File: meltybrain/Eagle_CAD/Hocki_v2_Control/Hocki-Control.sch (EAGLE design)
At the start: 152 parts, among them J1 SM03B-SRSS-TB(LF)(SN), J2 SM04B-SRSS-TB(LF)(SN), J3 SM02B-SRSS-TB(LF)(SN), J4 SM04B-SRSS-TB(LF)(SN), J5 SM03B-SRSS-TB(LF)(SN), J6 SM03B-SRSS-TB(LF)(SN), U1 AP63200, U10 LMH6612MAX/NOPB, U11 TLV3502AIDCNR, U12 LMH6612MAX/NOPB, U13 TMP235A4DCKR, U14 ADXL375, U15 NL27WZ32USG, U16 ADXL375, U17 ADXL375, U18 NL27WZ32USG, U19 ADXL375, U2 TEENSY_4.1, U20 LMV358, U21 LMV358, U22 HMC1052L-TR, U23 LMV358, U24 IRF7509, U3 AP2210K-5.0TRG1, U4 AP2210K-3.3TRG1, U5 74AHC1G04GW,125, U6 LDL212PU50R, U7 LMH6612MAX/NOPB, U8 LMH6612MAX/NOPB, U9 TMUX1219DCKR

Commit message: Moving v2 to a new directory to avoid merge conflicts and allow both versions to coexist in master
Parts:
- removed C52: 1000pF, rcl:C-USC0805
- removed J3: SM02B-SRSS-TB(LF)(SN), Hocki_Library:SM02B-SRSS-TB(LF)(SN)
- removed R37, R38, R41: 4.99k, rcl:R-US_R0603
- removed R42, R43, R44: 499k, rcl:R-US_R0603
- added C56: 0.1uF, rcl:C-USC0603
- added FB1: MPZ1608R391ATD25, Hocki_Library:MPZ1608R391ATD25
- added J7, J8: SM02B-SRSS-TB(LF)(SN), Hocki_Library:SM02B-SRSS-TB(LF)(SN)
- C44: value 1000pF -> 0.1uF; device rcl:C-USC0805 -> rcl:C-USC0603
- CN1: value (none) -> JST_2PIN
- R33: value 499k -> 49.9
- R36: value 4.99k -> 49.9
- U20: value LMV358 -> AD8426ACPZ-WP; device Hocki_Library:LMV358 -> Hocki_Library:AD8426ACPZ-WP
- U21, U23: value LMV358 -> LMH6612MAX/NOPB; device Hocki_Library:LMV358 -> Hocki_Library:LMH6612MAX/NOPB
- U5: value 74AHC1G04GW,125 -> TXS0104ED; device Hocki_Library:74AHC1G04GW,125 -> Hocki_Library:TXS0104ED
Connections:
- removed net LED_CLK1: J2.2, U2.2/PWM/OUT2
- removed net LED_DATA1: J2.3, U2.1/PWM/CTX2/MISO1/TX1
- removed net MAG_OUTPUTA: C44.2, R33.1, R34.2, U20.OUTA
- removed net MAG_OUTPUTB: C52.2, R39.2, R44.1, U20.OUTB
- removed net OUT+(A): R36.2, U22.OUT+(A)
- removed net OUT+(B): R38.2, U22.OUT+(B)
- removed net OUT-(A): R37.2, U22.OUT-(A)
- removed net OUT-(B): R41.2, U22.OUT-(B)
- removed net RC_SIGNAL: J1.1, U5.IN
- removed net SBUS: U2.0/PWM/CRX2/CS1/RX1, U5.OUT
- new net 3V3_LED_CLK: U2.2/PWM/OUT2, U5.A3
- new net 3V3_LED_DATA: U2.1/PWM/CTX2/MISO1/TX1, U5.A2
- new net 3V3_RC_SIGNAL: U2.0/PWM/CRX2/CS1/RX1, U5.A1
- new net 5V_LED_CLK: J2.2, J4.2, U5.B3
- new net 5V_LED_DATA: J2.3, J4.3, U5.B2
- new net 5V_RC_SIGNAL: J1.1, U5.B1
- new net ESC_TEL_L: J8.2, U2.28/PWM/RX7
- new net ESC_TEL_R: J7.1, U2.34/RX8
- new net N$28: C13.1, D13.C2, FB1.1, U4.OUT
- new net N$31: U20.INA+, U22.OUT+(A)
- new net N$32: U20.INA-, U22.OUT-(A)
- new net N$33: U20.INB+, U22.OUT+(B)
- new net N$38: R33.1, U20.RGA-
- new net N$39: R36.2, U20.RGB+
- new net N$40: R36.1, U20.RGB-
- net +3V3: now also C44.1, FB1.2; no longer C13.1, D13.C2, U4.OUT
- net 3.3V: now also U5.OE, U5.VCCA; no longer U5.VCC
- net 5V: now also C56.1, U5.VCCB
- net CS4: now also U2.25/PWM/SDA2/RX6/A11; no longer U2.24/PWM/SCL2/TX6/A10
- net ESC_L: now also J8.1, U2.29/PWM/TX7; no longer J3.1, U2.28/PWM/RX7
- net ESC_R: now also J7.2, U2.24/PWM/SCL2/TX6/A10; no longer J3.2, U2.29/PWM/TX7
- net GND: now also C44.2, C56.2, J7.SHIELD, J8.SHIELD; no longer J3.SHIELD
- net LED_CLK2: now also U2.3/PWM/LRCLK2; no longer J4.2, U2.4/PWM/BCLK2
- net LED_DATA2: now also U2.4/PWM/BCLK2; no longer J4.3, U2.3/PWM/LRCLK2
- net N$34: now also U22.OUT-(B); no longer R41.1, R43.1
- net N$35: now also R39.2, U20.OUTB; no longer C52.1, R38.1, R44.2, U20.INB+
- net N$36: now also R34.2, U20.OUTA; no longer R37.1, R42.1, U20.INA-
- net N$37: now also U20.RGA+; no longer C44.1, R36.1, U20.INA+
- net S/R: now also U2.33/PWM/MCLK2; no longer U2.32/OUT1B
- net VREF/2: now also U20.REFA, U20.REFB; no longer R42.2, R43.2
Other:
- note added: "ESC Connectors"
- note removed: "ESC Connector"
- note removed: "SBUS is inverted UART"
- moved on the sheet: C10, C11, C12, C13, C14, C15, C16, C17, C18, C44, C46, D10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

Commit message: add to sch
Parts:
- added U25: LIS3MDLTR, Hocki_Library:LIS3MDLTR
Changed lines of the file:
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@@
 <part name="GND83" library="SparkFun-PowerSymbols" deviceset="GND" device=""/>
 <part name="U5" library="Hocki_Library" deviceset="TXS0104ED" device=""/>
+<part name="U25" library="Hocki_Library" deviceset="LIS3MDLTR" device=""/>
 </parts>
 <sheets>
@@
 <attribute name="VALUE" x="184.15" y="173.482" size="1.778" layer="96" rot="R180"/>
 </instance>
+<instance part="U25" gate="A" x="198.12" y="134.62" smashed="yes">
+<attribute name="NAME" x="177.8" y="145.288" size="1.778" layer="95" ratio="6" rot="SR0"/>
+<attribute name="VALUE" x="177.8" y="123.952" size="1.778" layer="96" align="top-left"/>
+</instance>
 </instances>

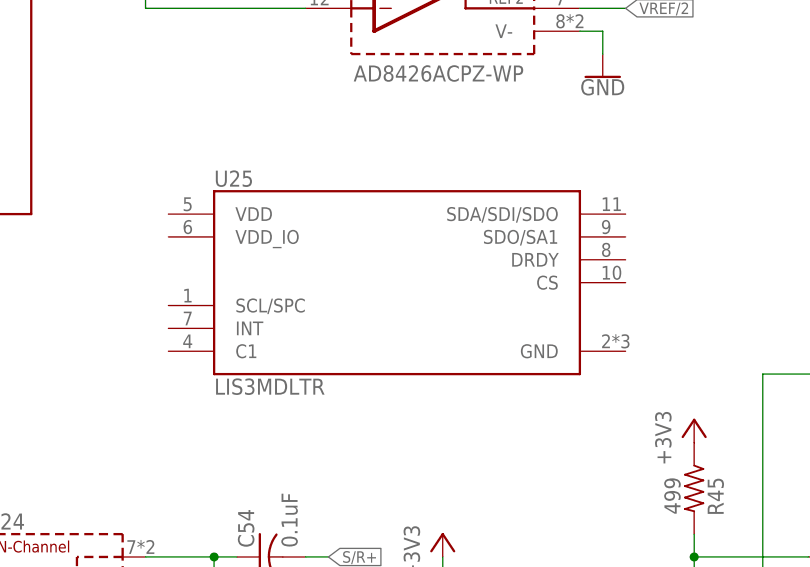
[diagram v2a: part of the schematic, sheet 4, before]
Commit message: route schematic for new magnetometer, remove IR capabilities and old magnetometer
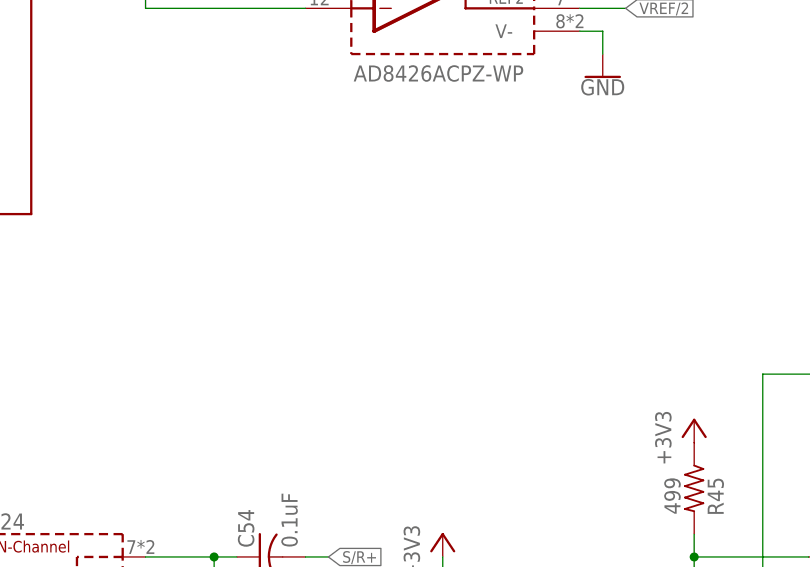
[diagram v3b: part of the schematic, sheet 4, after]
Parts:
- removed U25: LIS3MDLTR, Hocki_Library:LIS3MDLTR
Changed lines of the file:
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@@
 <part name="GND83" library="SparkFun-PowerSymbols" deviceset="GND" device=""/>
 <part name="U5" library="Hocki_Library" deviceset="TXS0104ED" device=""/>
-<part name="U25" library="Hocki_Library" deviceset="LIS3MDLTR" device=""/>
 </parts>
 <sheets>
@@
 <attribute name="VALUE" x="184.15" y="173.482" size="1.778" layer="96" rot="R180"/>
 </instance>
-<instance part="U25" gate="A" x="198.12" y="134.62" smashed="yes">
-<attribute name="NAME" x="177.8" y="145.288" size="1.778" layer="95" ratio="6" rot="SR0"/>
-<attribute name="VALUE" x="177.8" y="123.952" size="1.778" layer="96" align="top-left"/>
-</instance>
 </instances>
